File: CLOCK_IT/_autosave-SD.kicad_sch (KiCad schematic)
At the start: 9 parts, among them U3 AW9523BTQR

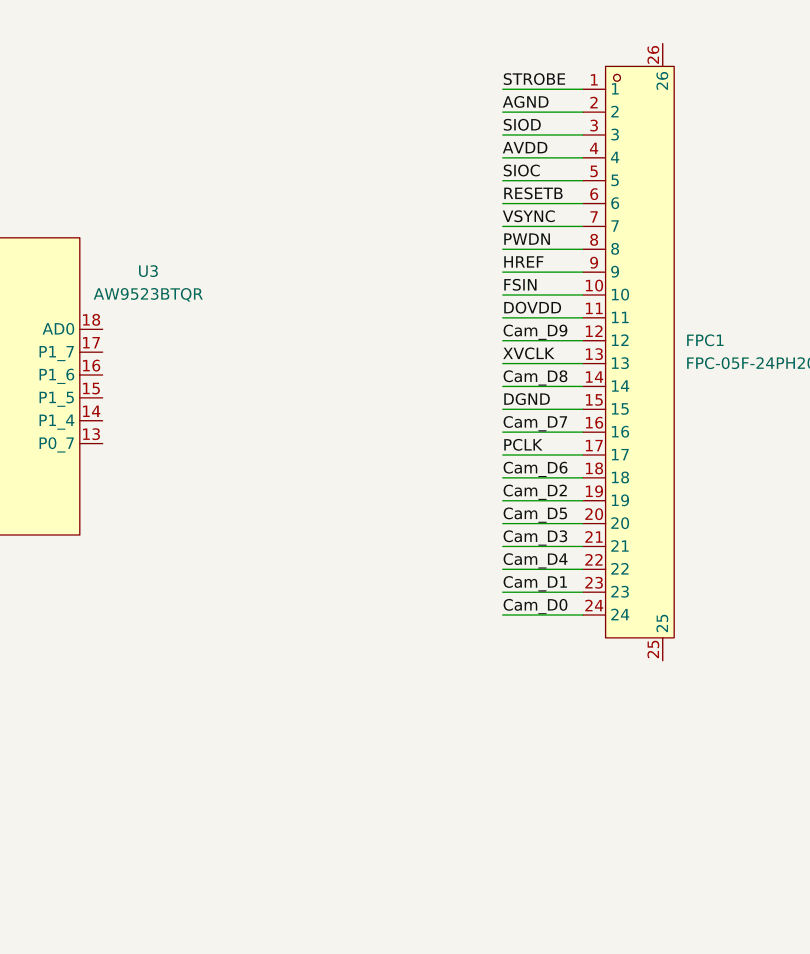
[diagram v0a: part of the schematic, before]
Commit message: :tada: added camera pin an pinout naming
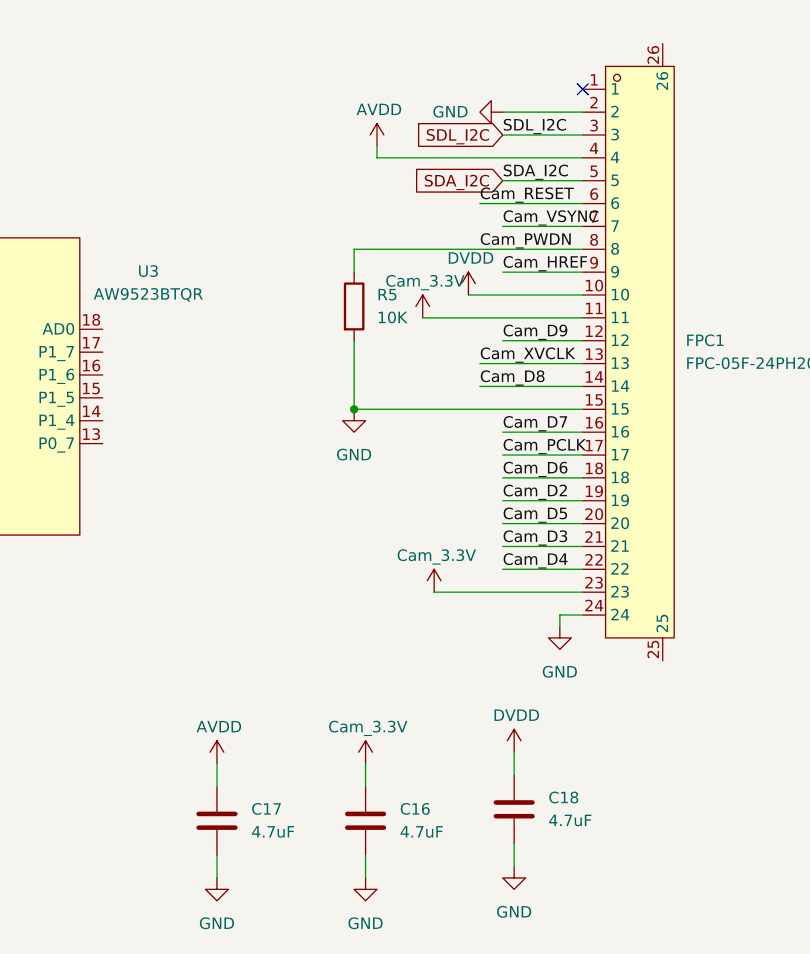
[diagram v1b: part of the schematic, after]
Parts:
- added C16, C17, C18: 4.7uF, symbol Device:C
- added R5: 10K, symbol Device:R
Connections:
- net AGND is gone; now on net GND: FPC1.2
- net Cam_D0 is gone; now on net GND: FPC1.24
- net DGND is gone; now on net GND: FPC1.15
- net DOVDD is gone; now on net Cam_3.3V: FPC1.11
- net AVDD: now also C17.1
- net GND: now also C16.2, C17.2, C18.2, R5.2
- net RESETB: no longer FPC1.6
- net Cam_D1 renamed Cam_3.3V
- net Cam_3.3V: now also C16.1
- net FSIN renamed DVDD
- net DVDD: now also C18.1
- net HREF renamed Cam_HREF
- net PCLK renamed Cam_PCLK
- net PWDN renamed Cam_PWDN
- net Cam_PWDN: now also R5.1
- net SIOC renamed SDA_I2C
- net SIOD renamed SDL_I2C
- net STROBE: no longer names the net of FPC1.1
- net VSYNC renamed Cam_VSYNC
- net XVCLK renamed Cam_XVCLK
- new net Cam_RESET: FPC1.6
- no-connect marks 5 -> 6
